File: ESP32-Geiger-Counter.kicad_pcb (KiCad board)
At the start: 2 copper layers, 137 x 84 mm, 85 parts, among them J1 2s1p Lipo Battery Pack (8.4V-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, J2 USB_C_Receptacle_USB2.0_16P, J5 Conn_01x07, Q1 STN1HNK60, Q3 2N7002, Q4 AO3401A, Q5 MMBT3904, SW1 SW_SPDT, U1 BQ25886RGE, U2 AP63203WU, U3 ESP32-S3-WROOM-1, U4 UCC27517DBVR, U5 USBLC6-2SC6, U6 SBM-20 Geiger Mueller Tube

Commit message: added test points
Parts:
- added TP_3.3V1: 3.3V, TestPoint:TestPoint_Keystone_5015_Micro_Mini, F.Cu at (195.4, 263.4)
- added TP_GND1: GND, TestPoint:TestPoint_Keystone_5015_Micro_Mini, F.Cu at (229.9, 291.6)
- added TP_HV_SENSE1: HV_SENSE, TestPoint:TestPoint_Keystone_5015_Micro_Mini, F.Cu at (217.1, 273.9)
- added TP_PULSE1: PULSE, TestPoint:TestPoint_Keystone_5015_Micro_Mini, F.Cu at (207.2, 242.7)
- renumbered RESET to SW2, BOOT to SW3
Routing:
- net /PULSE: track 12.1 -> 18.7 mm
- net +3.3V: track 157.6 -> 162.8 mm
- net /HV_SENSE: track 135.7 -> 139.8 mm
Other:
- board text added: "400V High Voltage"

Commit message: minor changes
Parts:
- moved TP_3.3V1 0.86 mm to (194.7, 263.9)
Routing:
- net +3.3V: track 162.8 -> 161.9 mm
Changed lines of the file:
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@@
 	(footprint "TestPoint:TestPoint_Keystone_5015_Micro_Mini"
 		(layer "F.Cu")
-		(at 195.4 263.4 90)
+		(at 194.7 263.9 90)
 		(descr "Keystone SMT Micro Mini Test Point 5015, http://www.keyelco.com/product-pdf.cfm?p=1353")
 		(tags "Test Point")
@@
 	)
 	(segment
-		(start 181.8 261.6)
-		(end 182.1 261.9)
-		(width 1)
+		(start 194.7 263.9)
+		(end 192.7 265.9)
+		(width 0.3)
 		(layer "F.Cu")
 		(net "+3.3V")
 	)
 	(segment
-		(start 182.1 261.7)
+		(start 181.8 261.6)
 		(end 182.1 261.9)
 		(width 1)
@@
 	)
 	(segment
-		(start 192.9 265.9)
-		(end 195.4 263.4)
-		(width 0.3)
+		(start 182.1 261.7)
+		(end 182.1 261.9)
+		(width 1)
 		(layer "F.Cu")
 		(net "+3.3V")
@@
 	)
 	(segment
-		(start 191.225 265.9)
-		(end 192.9 265.9)
-		(width 0.3)
-		(layer "F.Cu")
-		(net "+3.3V")
-	)
-	(segment
 		(start 191.225 260.3)
 		(end 191.225 265.9)
@@
 		(width 0.3)
 		(layer "F.Cu")
+		(net "+3.3V")
+	)
+	(segment
+		(start 192.7 265.9)
+		(end 191.225 265.9)
+		(width 0.3)
+		(layer "F.Cu")

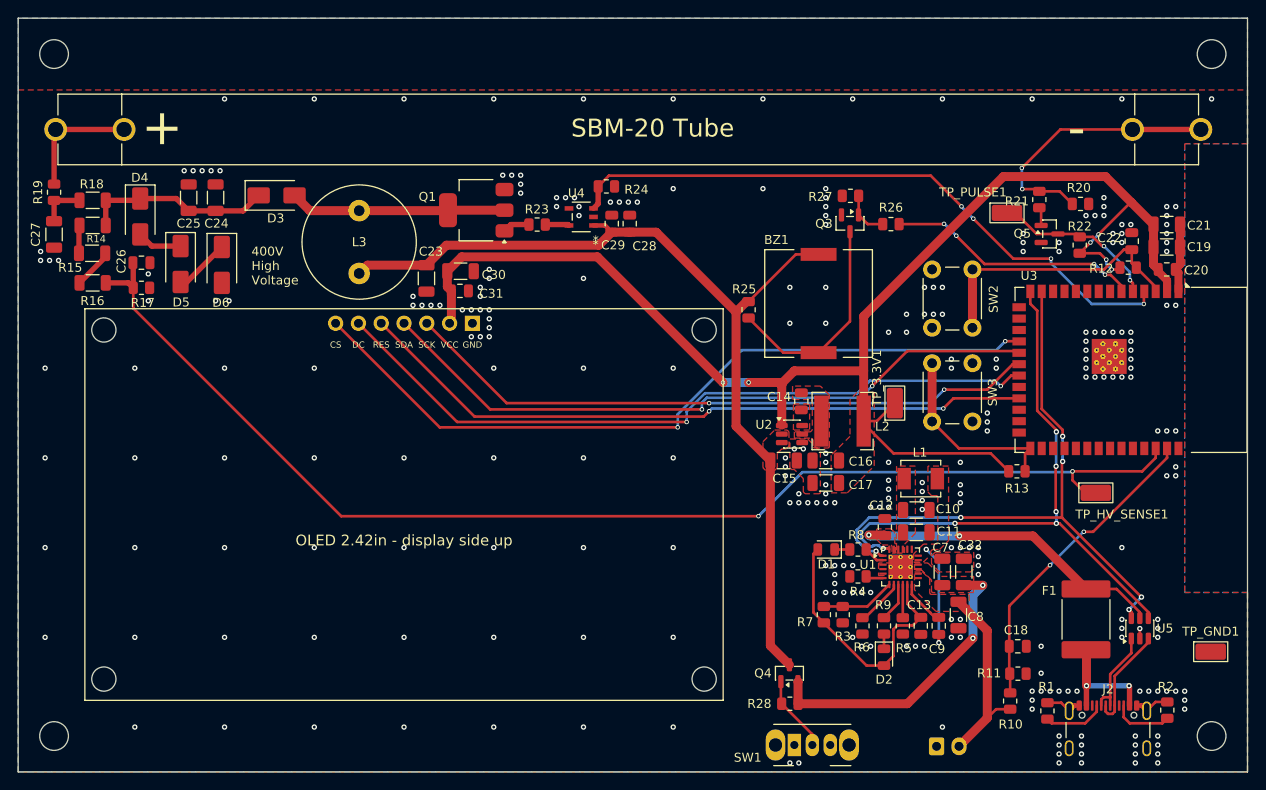
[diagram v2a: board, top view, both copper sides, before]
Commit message: pour changes, fixed bad sbm-20 tube footprint
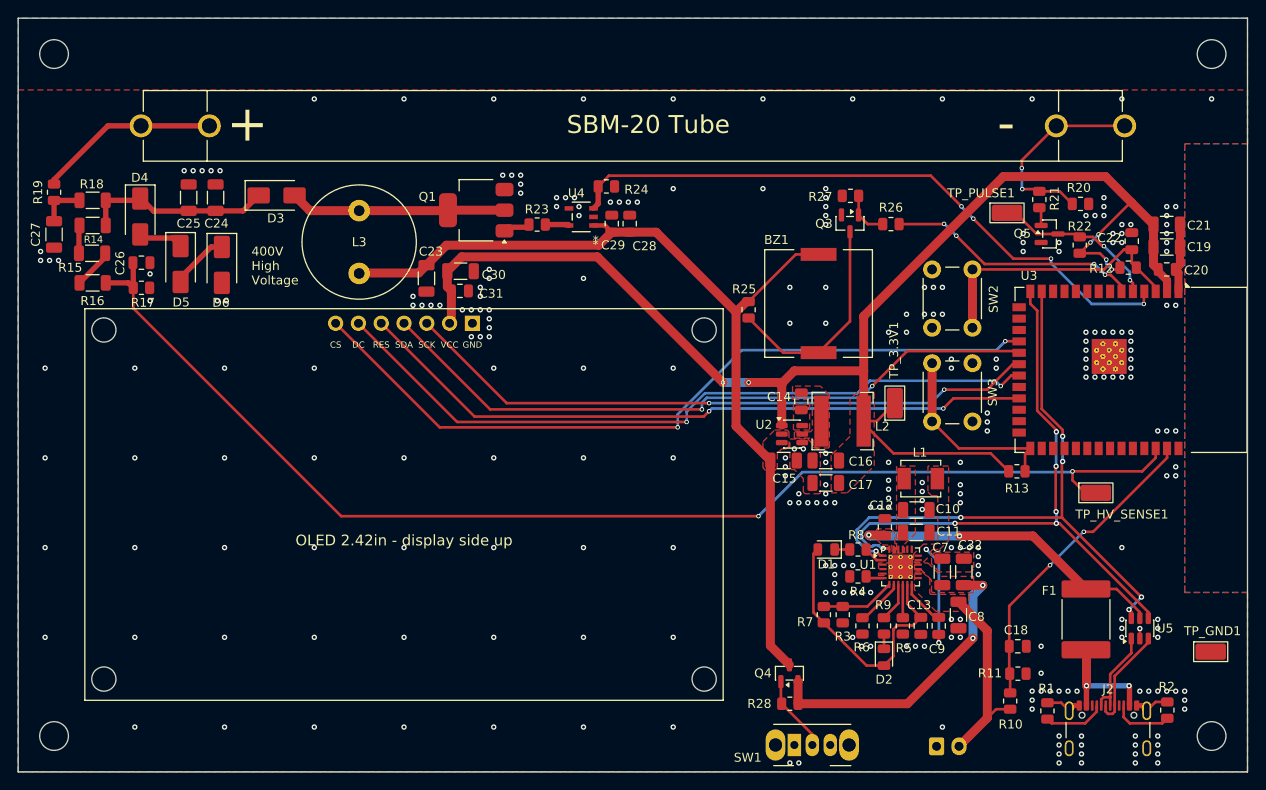
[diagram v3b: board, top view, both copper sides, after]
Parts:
- R5: value 5.76K -> 3.83k
- moved U6 61.6 mm to (165.5, 233.0)
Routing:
- net Net-(U6-K): track 30.4 -> 22.5 mm
- net Net-(U6-A): track 13.8 -> 20.3 mm
- net GND: vias 280 -> 279

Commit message: minor passive changes
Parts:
- R19: footprint Resistor_SMD:R_0805_2012Metric -> Resistor_SMD:R_1206_3216Metric
- moved D3 1.98 mm to (124.7, 242.4)
- moved L3 0.66 mm to (134.9, 248.8)
- moved R19 0.20 mm to (101.0, 240.2)
- moved R14 0.20 mm to (105.5, 244.1)
- moved R15 0.20 mm to (105.4, 247.2)
- moved R16 0.20 mm to (105.5, 250.5)
- moved R18 0.20 mm to (105.5, 241.3)
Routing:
- net Net-(D3-K): track 21.2 -> 19.5 mm
- net Net-(D3-A): track 24.1 -> 25.1 mm
- net Net-(U6-A): track 20.3 -> 19.7 mm
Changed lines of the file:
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@@
 	(footprint "Inductor_THT:L_Radial_D12.5mm_P7.00mm_Fastron_09HCP"
 		(layer "F.Cu")
-		(at 135 249.45 90)
+		(at 134.9 248.8 90)
 		(descr "Inductor, Radial series, Radial, pin pitch=7.00mm, diameter=12.5mm, height=10.8mm, Fastron, 09HCP, http://cdn-reichelt.de/documents/datenblatt/B400/DS_09HCP.pdf")
 		(tags "Inductor Radial series Radial pin pitch 7.00mm  diameter 12.5mm height 10.8mm Fastron 09HCP")
@@
 	(footprint "Resistor_SMD:R_1206_3216Metric"
 		(layer "F.Cu")
-		(at 105.3 244.1)
+		(at 105.5 244.1)
 		(descr "Resistor SMD 1206 (3216 Metric), square (rectangular) end terminal, IPC-7351 nominal, (Body size source: IPC-SM-782 page 72, https://www.pcb-3d.com/wordpress/wp-content/uploads/ipc-sm-782a_amendment_1_and_2.pdf)")
 		(tags "resistor")
 		(property "Reference" "R14"
-			(at 0.088759 1.566506 0)
+			(at 0 1.5 0)
 			(layer "F.SilkS")
 			(effects
@@
 	(footprint "Resistor_SMD:R_1206_3216Metric"
 		(layer "F.Cu")
-		(at 105.3 250.5 180)
+		(at 105.5 250.5 180)
 		(descr "Resistor SMD 1206 (3216 Metric), square (rectangular) end terminal, IPC-7351 nominal, (Body size source: IPC-SM-782 page 72, https://www.pcb-3d.com/wordpress/wp-content/uploads/ipc-sm-782a_amendment_1_and_2.pdf)")
 		(tags "resistor")
@@
 	(footprint "Resistor_SMD:R_1206_3216Metric"
 		(layer "F.Cu")
-		(at 105.3 241.3 180)
+		(at 105.5 241.3 180)
 		(descr "Resistor SMD 1206 (3216 Metric), square (rectangular) end terminal, IPC-7351 nominal, (Body size source: IPC-SM-782 page 72, https://www.pcb-3d.com/wordpress/wp-content/uploads/ipc-sm-782a_amendment_1_and_2.pdf)")
 		(tags "resistor")
@@
 	(footprint "Diode_SMD:D_SMA"
 		(layer "F.Cu")
-		(at 125.8 240.75)
+		(at 124.7 242.4)
 		(descr "Diode SMA (DO-214AC)")
 		(tags "Diode SMA (DO-214AC)")
 		(property "Reference" "D3"
-			(at -0.1 2.55 0)
+			(at -0.1 -2.4 0)
 			(layer "F.SilkS")
 			(effects
@@
 		)
 	)
-	(footprint "Resistor_SMD:R_0805_2012Metric"
+	(footprint "Resistor_SMD:R_1206_3216Metric"
 		(layer "F.Cu")
-		(at 101 240.4 90)
-		(descr "Resistor SMD 0805 (2012 Metric), square (rectangular) end terminal, IPC-7351 nominal, (Body size source: IPC-SM-782 page 72, https://www.pcb-3d.com/wordpress/wp-content/uploads/ipc-sm-782a_amendment_1_and_2.pdf)")
+		(at 101 240.2 90)
+		(descr "Resistor SMD 1206 (3216 Metric), square (rectangular) end terminal, IPC-7351 nominal, (Body size source: IPC-SM-782 page 72, https://www.pcb-3d.com/wordpress/wp-content/uploads/ipc-sm-782a_amendment_1_and_2.pdf)")
 		(tags "resistor")
 		(property "Reference" "R19"
-			(at 0.004401 -1.791188 90)
+			(at 0 -1.83 90)
 			(layer "F.SilkS")
 			(effects
@@
 		)
 		(property "Value" "5.1M"
-			(at 0 1.65 90)
+			(at 0 1.83 90)
 			(layer "F.Fab")
 			(effects
@@
 		(duplicate_pad_numbers_are_jumpers no)
 		(fp_line
-			(start -0.227064 -0.735)
-			(end 0.227064 -0.735)
+			(start -0.727064 -0.91)
+			(end 0.727064 -0.91)
 			(stroke
 				(width 0.12)
@@
 		)
 		(fp_line
-			(start -0.227064 0.735)
-			(end 0.227064 0.735)
+			(start -0.727064 0.91)
+			(end 0.727064 0.91)
 			(stroke
 				(width 0.12)
@@
 		)
 		(fp_rect
-			(start -1.68 -0.95)
-			(end 1.68 0.95)
+			(start -2.28 -1.13)
+			(end 2.28 1.13)
 			(stroke
 				(width 0.05)
@@
 		)
 		(fp_rect
-			(start -1 -0.625)
-			(end 1 0.625)
+			(start -1.6 -0.8)
+			(end 1.6 0.8)
 			(stroke
 				(width 0.1)
@@
 			(effects
 				(font
-					(size 0.5 0.5)
-					(thickness 0.08)
+					(size 0.8 0.8)
+					(thickness 0.12)
 				)
 			)
 		)
 		(pad "1" smd roundrect
-			(at -0.9125 0 90)
-			(size 1.025 1.4)
+			(at -1.4625 0 90)
+			(size 1.125 1.75)
 			(layers "F.Cu" "F.Mask" "F.Paste")
-			(roundrect_rratio 0.243902)
+			(roundrect_rratio 0.222222)
 			(net "Net-(C27-Pad1)")
 			(pintype "passive")
 		)
 		(pad "2" smd roundrect
-			(at 0.9125 0 90)
-			(size 1.025 1.4)
+			(at 1.4625 0 90)
+			(size 1.125 1.75)
 			(layers "F.Cu" "F.Mask" "F.Paste")
-			(roundrect_rratio 0.243902)
+			(roundrect_rratio 0.222222)
 			(net "Net-(U6-A)")
 			(pintype "passive")
 		)
 		(embedded_fonts no)
-		(model "${KICAD10_3DMODEL_DIR}/Resistor_SMD.3dshapes/R_0805_2012Metric.step"
+		(model "${KICAD10_3DMODEL_DIR}/Resistor_SMD.3dshapes/R_1206_3216Metric.step"
 			(offset
 				(xyz 0 0 0)
@@
 	(footprint "Resistor_SMD:R_1206_3216Metric"
 		(layer "F.Cu")
-		(at 105.2375 247.2 180)
+		(at 105.4375 247.2 180)
 		(descr "Resistor SMD 1206 (3216 Metric), square (rectangular) end terminal, IPC-7351 nominal, (Body size source: IPC-SM-782 page 72, https://www.pcb-3d.com/wordpress/wp-content/uploads/ipc-sm-782a_amendment_1_and_2.pdf)")
 		(tags "resistor")
 		(property "Reference" "R15"
-			(at 2.4375 -1.6 0)
+			(at 1.6375 -1.6 0)
 			(layer "F.SilkS")
 			(effects
@@
 	)
 	(segment
+		(start 142.5 248.525)
+		(end 135.175 248.525)
+		(width 1)
+		(layer "F.Cu")
+		(net "/VSYS_SW")
+	)
+	(segment
 		(start 177 253.75)
 		(end 177 266.475)
@@
 	)
 	(segment
+		(start 135.175 248.525)
+		(end 134.9 248.8)
+		(width 1)
+		(layer "F.Cu")
+		(net "/VSYS_SW")
+	)
+	(segment
 		(start 180.825 290.9375)
 		(end 182.95 293.0625)
@@
 	)
 	(segment
-		(start 141.625 249.4)
-		(end 135.05 249.4)
-		(width 1)
-		(layer "F.Cu")
-		(net "/VSYS_SW")
-	)
-	(segment
-		(start 142.5 248.525)
-		(end 141.625 249.4)
-		(width 1)
-		(layer "F.Cu")
-		(net "/VSYS_SW")
-	)
-	(segment
 		(start 183.6625 247.325)
 		(end 178.4 252.5875)
@@
 	)
 	(segment
+		(start 126.75 242.45)
+		(end 126.7 242.4)
+		(width 1)
+		(layer "F.Cu")
+		(net "Net-(D3-A)")
+	)
+	(segment
 		(start 144.85 242.45)
 		(end 144.9 242.4)
@@
 	)
 	(segment
-		(start 135 242.45)
-		(end 144.85 242.45)
+		(start 127.3 241.8)
+		(end 126.7 242.4)
+		(width 1)
+		(layer "F.Cu")
+		(net "Net-(D3-A)")
+	)
+	(segment
+		(start 135.5 242.4)
+		(end 134.9 241.8)
 		(width 1)
 		(layer "F.Cu")
@@
 	)
 	(segment
-		(start 129.5 242.45)
-		(end 127.8 240.75)
+		(start 144.9 242.4)
+		(end 135.5 242.4)
 		(width 1)
 		(layer "F.Cu")
@@
 	)
 	(segment
-		(start 135 242.45)
-		(end 129.5 242.45)
+		(start 134.9 241.8)
+		(end 127.3 241.8)
 		(width 1)
 		(layer "F.Cu")
@@
 	)
 	(segment
-		(start 223.767229 269.996992)
-		(end 223.767229 268.946992)
-		(width 0.3)
+		(start 109.275 250.5)
+		(end 109.825 251.05)
+		(width 0.6)
 		(layer "F.Cu")
 		(net "/HV_SENSE")
 	)
 	(segment
-		(start 106.7625 250.5)
-		(end 109.275 250.5)
-		(width 0.6)
+		(start 223.767229 269.996992)
+		(end 223.767229 268.946992)
+		(width 0.3)
 		(layer "F.Cu")
 		(net "/HV_SENSE")
 	)
 	(segment
-		(start 109.275 250.5)
-		(end 109.825 251.05)
+		(start 106.9625 250.5)
+		(end 109.275 250.5)
 		(width 0.6)
 		(layer "F.Cu")
@@
 	)
 	(segment
-		(start 101 241.3125)
-		(end 103.825 241.3125)
+		(start 103.825 241.3125)
+		(end 103.8375 241.3)
 		(width 0.6)
 		(layer "F.Cu")
@@
 	)
 	(segment
-		(start 103.825 241.3125)
-		(end 103.8375 241.3)
-		(width 0.6)
+		(start 101 241.6625)
+		(end 103.675 241.6625)
+		(width 0.3)
 		(layer "F.Cu")
 		(net "Net-(C27-Pad1)")
 	)
 	(segment
-		(start 101 243.625)
-		(end 101 241.3125)
-		(width 0.6)
+		(start 101 241.6625)
+		(end 101 243.625)
+		(width 0.3)
+		(layer "F.Cu")
+		(net "Net-(C27-Pad1)")
+	)
+	(segment
+		(start 103.675 241.6625)
+		(end 104.0375 241.3)
+		(width 0.3)
 		(layer "F.Cu")
 		(net "Net-(C27-Pad1)")
@@
 	)
 	(segment
-		(start 103.775 247.2)
-		(end 103.775 244.1625)
+		(start 103.975 247.2)
+		(end 103.975 244.1625)
 		(width 0.6)
 		(layer "F.Cu")
@@
 	)
 	(segment
-		(start 106.7625 241.3)
-		(end 106.7625 244.1)
-		(width 0.6)
-		(layer "F.Cu")
-		(net "Net-(D3-K)")
-	)
-	(segment
-		(start 112.1 242.5)
-		(end 115.975 242.5)
+		(start 107.1625 241.1)
+		(end 106.9625 241.3)
 		(width 0.6)
 		(layer "F.Cu")
@@
 	)
 	(segment
-		(start 123.8 240.75)
-		(end 122.075 242.475)
+		(start 122.7 242.4)
+		(end 119.075 242.4)
 		(width 0.6)
 		(layer "F.Cu")
@@
 	)
 	(segment
-		(start 122.075 242.475)
-		(end 119 242.475)
+		(start 112.1 242.5)
+		(end 115.975 242.5)
 		(width 0.6)
 		(layer "F.Cu")
@@
 	)
 	(segment
-		(start 106.7625 241.3)
-		(end 110.4 241.3)
+		(start 106.9625 241.3)
+		(end 106.9625 244.1)
 		(width 0.6)
 		(layer "F.Cu")
@@
 	)
 	(segment
+		(start 119.075 242.4)
+		(end 119 242.475)
+		(width 0.6)
+		(layer "F.Cu")
+		(net "Net-(D3-K)")
+	)
+	(segment
+		(start 110.6 241.1)
+		(end 107.1625 241.1)
+		(width 0.6)
+		(layer "F.Cu")
+		(net "Net-(D3-K)")
+	)
+	(segment
 		(start 110.6 241.1)
 		(end 110.7 241.1)
@@
 	)
 	(segment
-		(start 106.7 247.6375)
-		(end 103.8375 250.5)
+		(start 106.9 247.6375)
+		(end 104.0375 250.5)
 		(width 0.6)
 		(layer "F.Cu")
@@
 	)
 	(segment
-		(start 107 233)
-		(end 110.69 233)
+		(start 106.7375 233)
+		(end 101 238.7375)
 		(width 0.6)
 		(layer "F.Cu")
@@
 	)
 	(segment
-		(start 101 239.4875)
-		(end 101 239)
-		(width 0.6)
-		(layer "F.Cu")
-		(net "Net-(U6-A)")
-	)
-	(segment
-		(start 101 239)
-		(end 107 233)
+		(start 110.69 233)
+		(end 106.7375 233)
 		(width 0.6)
 		(layer "F.Cu")
@@
 				(xy 129.3 238.1) (xy 129.3 235.4) (xy 150.1 235.4) (xy 150.1 240.9) (xy 156 240.9) (xy 156 248)
 				(xy 146 248) (xy 146 250.9) (xy 140.4 250.9) (xy 140.4 253) (xy 120.7 253) (xy 120.7 249.2) (xy 118.7 249.2)
-				(xy 118.7 253) (xy 112.3 253) (xy 112.3 247.5) (xy 111.1 247.5) (xy 111.1 253) (xy 102 253) (xy 102 246)
+				(xy 118.7 253) (xy 112.3 253) (xy 112.3 247.5) (xy 111.1 247.5) (xy 111.1 253) (xy 101.9 253) (xy 101.9 246)
 				(xy 97 246)
 			)

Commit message: pre via stiching
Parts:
- C26: value 10nF -> 2.2nF
- moved D4 1.60 mm to (110.7, 241.5)
- moved D5 0.70 mm to (115.1, 247.7)
- moved D6 0.70 mm to (119.7, 247.8)
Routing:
- net Net-(D3-K): track 19.5 -> 20.9 mm
- net GND: vias 279 -> 220

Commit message: saving now
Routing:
- net GND: vias 220 -> 516

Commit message: small text changes
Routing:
- net GND: vias 516 -> 520
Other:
- board text added: "Avalanche32"
- board text added: "ESP32-S3 Geiger Counter · Aron Szucs · Rev A · 2026"
- board text removed: "Avalanche32 by Aron Szucs"

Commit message: more vias
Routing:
- net GND: vias 520 -> 562
